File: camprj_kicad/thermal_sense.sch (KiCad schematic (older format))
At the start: 20 parts, among them U1 LM3670SOT23-5, U2 Molex 1052028-1001, U3 ADP150AUJZ-3.3-R7, U4 ADP150AUJZ-2.8-R7, Y1 ASFLMB-25MHZ

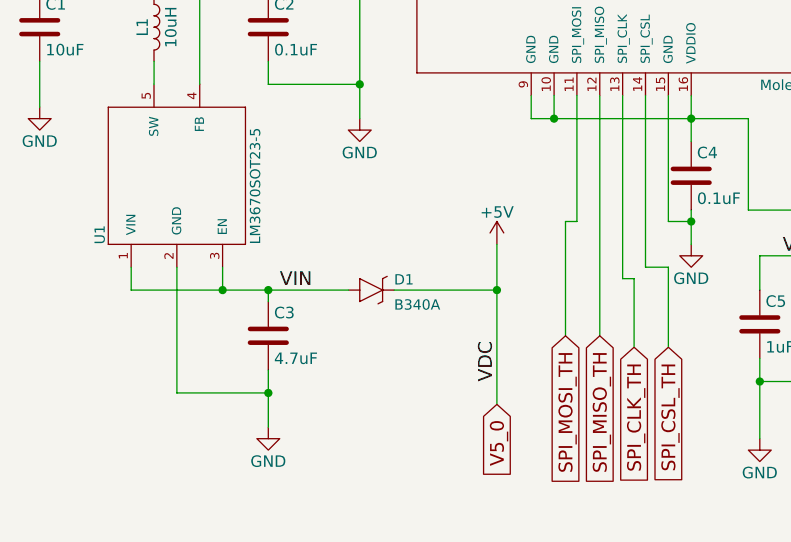
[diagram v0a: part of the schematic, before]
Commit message: Board design: component placement done
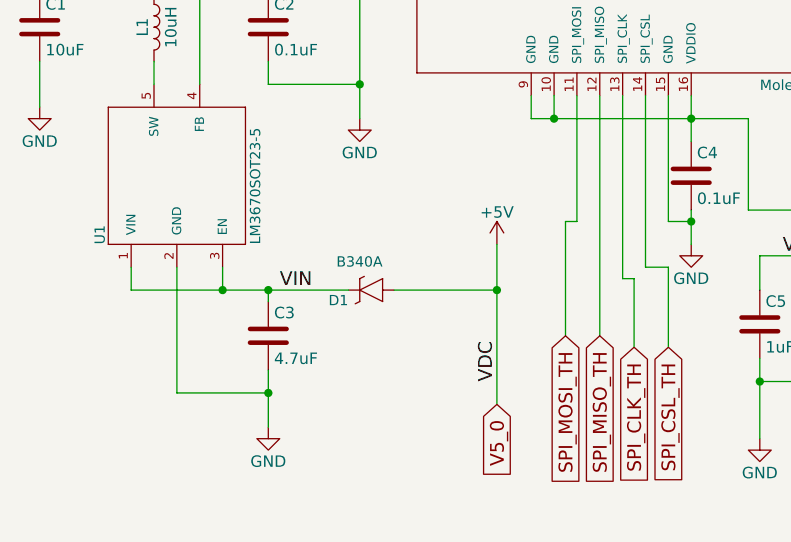
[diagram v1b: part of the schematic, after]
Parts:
- D1: Buy Link (none) -> http://www.mouser.ch/ProductDetail/Diodes-Incorporated/B340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
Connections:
- net +5V: now also D1.A; no longer D1.C
- net VIN: now also D1.C; no longer D1.A
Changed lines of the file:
@@
 EESchema Schematic File Version 2
+LIBS:camprj_kicad-rescue
 LIBS:power
 LIBS:device
@@
 	1    0    0    -1
 $EndComp
-$Comp
-L SCHOTTKY-B340A D1
-U 1 1 595E85D3
-P 3750 5000
-F 0 "D1" H 3850 5019 45  0000 L BNN
-F 1 "B340A" H 3850 4909 45  0000 L BNN
-F 2 "Myfootprints:D_SMA_Handsoldering_AC" H 3780 5150 20  0001 C CNN
-F 3 "" H 3850 5019 60  0001 C CNN
-	1    3750 5000
-	1    0    0    -1
-$EndComp
 Text Label 4300 5400 1    60   ~ 0
 VDC
@@
 Wire Wire Line
 	2850 3250 2850 3450
+$Comp
+L SCHOTTKY-B340A D1
+U 1 1 5974B1F1
+P 3750 5000
+F 0 "D1" H 3850 5019 45  0000 L BNN
+F 1 "B340A" H 3700 4850 45  0000 L BNN
+F 2 "Myfootprints:D_SMA_Handsoldering_AC" H 3780 5150 20  0001 C CNN
+F 3 "http://www.mouser.com/ds/2/115/ds30891-89887.pdf" H 3850 5019 60  0001 C CNN
+F 4 "http://www.mouser.ch/ProductDetail/Diodes-Incorporated/B340A-13-F/?qs=aLaTXeBcTP9fj%2fYKVo6Q1A==" H 3950 5119 60  0001 C CNN "Buy Link"
+	1    3750 5000
+	-1   0    0    1
+$EndComp
 $EndSCHEMATC

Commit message: routing done
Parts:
- U2: footprint 105028-1001:105028-1001 -> Myfootprints:105028-1001
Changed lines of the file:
@@
 F 0 "U2" H 3960 4180 45  0000 L BNN
 F 1 "Molex 1052028-1001" H 5450 2570 45  0000 L BNN
-F 2 "105028-1001:105028-1001" H 4880 3500 20  0001 C CNN
+F 2 "Myfootprints:105028-1001" H 4880 3500 20  0001 C CNN
 F 3 "http://www.mouser.com/ds/2/276/1050281001_OTHER_SOCKETS-152362.pdf" H 4850 3350 60  0001 C CNN
 F 4 "http://eu.mouser.com/ProductDetail/Molex/105028-1001/?qs=3OKVfsn1b5DSpyA99lGNjg%3D%3D" H 4850 3350 60  0001 C CNN "Buy Link"

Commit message: Final Delivery
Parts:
- D1: MPN (none) -> B340A-13-F
- U1: MPN (none) -> LM3670MFX-ADJ/NOPB
- U2: MPN (none) -> 105028-1001
- U3: MPN (none) -> ADP150AUJZ-3.3-R7
- U4: MPN (none) -> ADP150AUJZ-2.8-R7
- Y1: MPN (none) -> ASFLMB-25.000MHZ-LC-T
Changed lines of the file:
@@
 Date "2017-07-06"
 Rev "1"
-Comp "D-HEST, ETH Zurich"
+Comp "MHSL ETH Zurich"
 Comment1 "Geethan Karunaratne"
 Comment2 ""
@@
 F 3 "http://www.mouser.com/ds/2/276/1050281001_OTHER_SOCKETS-152362.pdf" H 4850 3350 60  0001 C CNN
 F 4 "http://eu.mouser.com/ProductDetail/Molex/105028-1001/?qs=3OKVfsn1b5DSpyA99lGNjg%3D%3D" H 4850 3350 60  0001 C CNN "Buy Link"
+F 5 "105028-1001" H 4850 3350 60  0001 C CNN "MPN"
 	1    4850 3350
 	1    0    0    -1
@@
 F 3 "http://www.ti.com/lit/ds/symlink/lm3670.pdf" H 2900 4500 60  0001 C CNN
 F 4 "http://eu.mouser.com/ProductDetail/Texas-Instruments/LM3670MFX-ADJ-NOPB/?qs=sGAEpiMZZMsMIqGZiACxIYreuZyZ6HSrgrP8lU6%252bpXc%3d" H 2900 4500 60  0001 C CNN "Buy Link"
+F 5 "LM3670MFX-ADJ/NOPB" H 2900 4500 60  0001 C CNN "MPN"
 	1    2900 4500
 	0    -1   -1   0
@@
 F 3 "http://www.mouser.com/ds/2/3/ASFLMB-24525.pdf" H 6550 1850 60  0001 C CNN
 F 4 "http://eu.mouser.com/ProductDetail/ABRACON/ASFLMB-25000MHZ-LC-T/?qs=3YAjQa1E1OmYZx%252blyx8lOg%3D%3D" H 6550 1850 60  0001 C CNN "Buy Link"
+F 5 "ASFLMB-25.000MHZ-LC-T" H 6550 1850 60  0001 C CNN "MPN"
 	1    6550 1850
 	-1   0    0    1
@@
 F 3 "http://www.mouser.com/ds/2/609/ADP150-773560.pdf" H 7850 4000 60  0001 C CNN
 F 4 "http://eu.mouser.com/ProductDetail/Analog-Devices/ADP150AUJZ-28-R7/?qs=WIvQP4zGanh7WlpvNfrmXw%3D%3D" H 7850 4000 60  0001 C CNN "Buy Link"
+F 5 "ADP150AUJZ-2.8-R7" H 7850 4000 60  0001 C CNN "MPN"
 	1    7850 4000
 	-1   0    0    -1
@@
 F 3 "http://www.mouser.com/ds/2/609/ADP150-773560.pdf" H 6250 5050 60  0001 C CNN
 F 4 "http://eu.mouser.com/ProductDetail/Analog-Devices/ADP150AUJZ-33-R7/?qs=WIvQP4zGanjNlX1MqHWsFA%3D%3D" H 6250 5050 60  0001 C CNN "Buy Link"
+F 5 "ADP150AUJZ-3.3-R7" H 6250 5050 60  0001 C CNN "MPN"
 	1    6250 5050
 	1    0    0    -1
@@
 F 3 "http://www.mouser.com/ds/2/115/ds30891-89887.pdf" H 3850 5019 60  0001 C CNN
 F 4 "http://www.mouser.ch/ProductDetail/Diodes-Incorporated/B340A-13-F/?qs=aLaTXeBcTP9fj%2fYKVo6Q1A==" H 3950 5119 60  0001 C CNN "Buy Link"
+F 5 "B340A-13-F" H 3750 5000 60  0001 C CNN "MPN"
 	1    3750 5000
 	-1   0    0    1
